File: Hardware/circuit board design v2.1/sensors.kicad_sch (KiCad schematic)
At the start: 10 parts, among them U4 BME280, U8 BMI088, U9 LIS3MDLTR

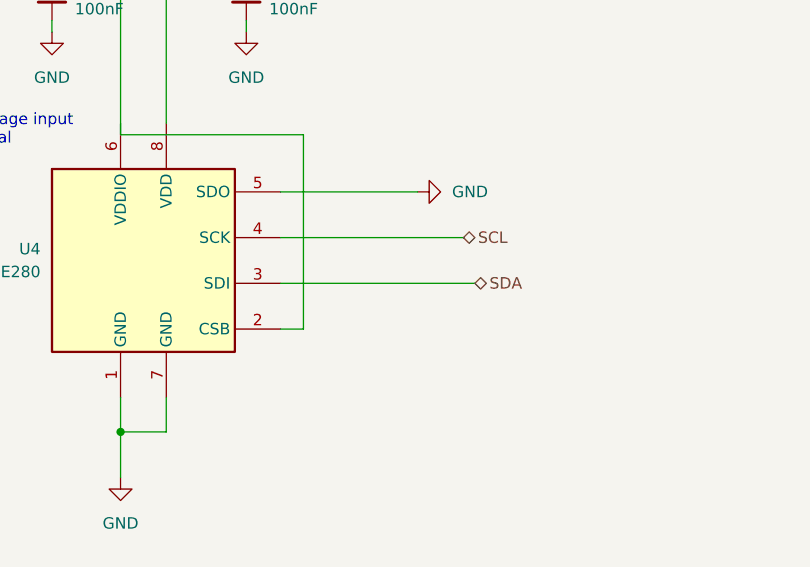
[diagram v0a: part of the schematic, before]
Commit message: Found error transistor pinout
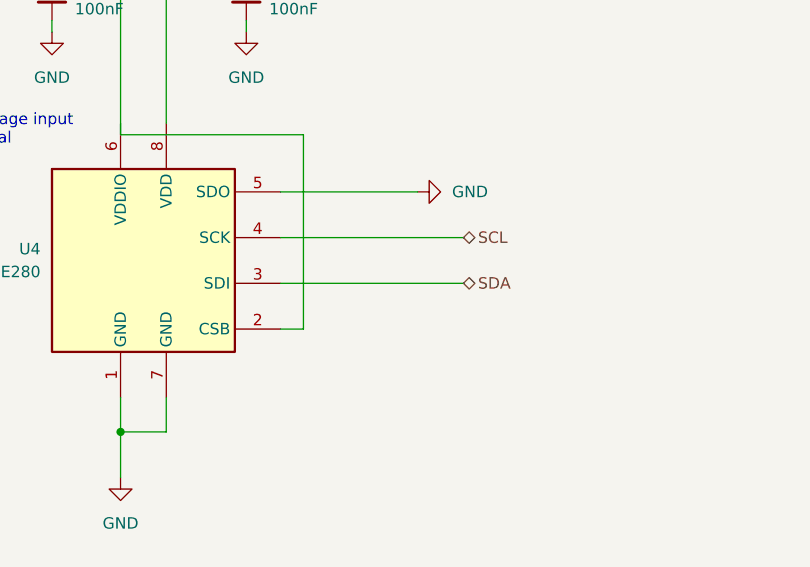
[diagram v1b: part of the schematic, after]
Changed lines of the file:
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@@
     (stroke (width 0) (type default) (color 0 0 0 0))
   )
-  (wire (pts (xy 73.66 67.31) (xy 95.25 67.31))
+  (wire (pts (xy 73.66 67.31) (xy 93.98 67.31))
     (stroke (width 0) (type default) (color 0 0 0 0))
   )
@@
     (effects (font (size 1.27 1.27)) (justify left))
   )
-  (hierarchical_label "SDA" (shape bidirectional) (at 95.25 67.31 0)
+  (hierarchical_label "SDA" (shape bidirectional) (at 93.98 67.31 0)
     (effects (font (size 1.27 1.27)) (justify left))
   )

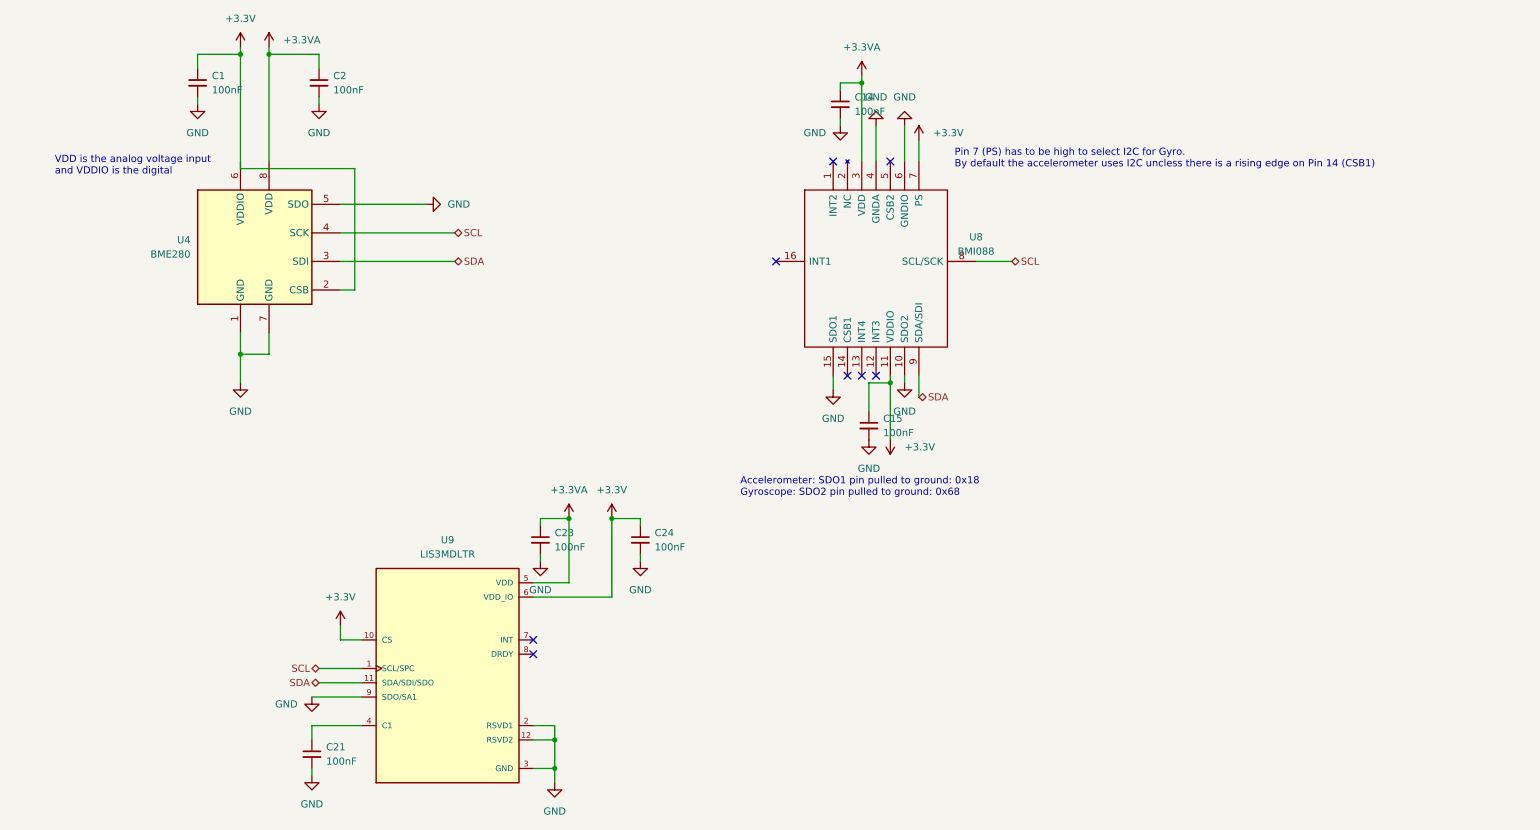
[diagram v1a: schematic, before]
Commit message: Added interupt pins to from BMI088 and LIS
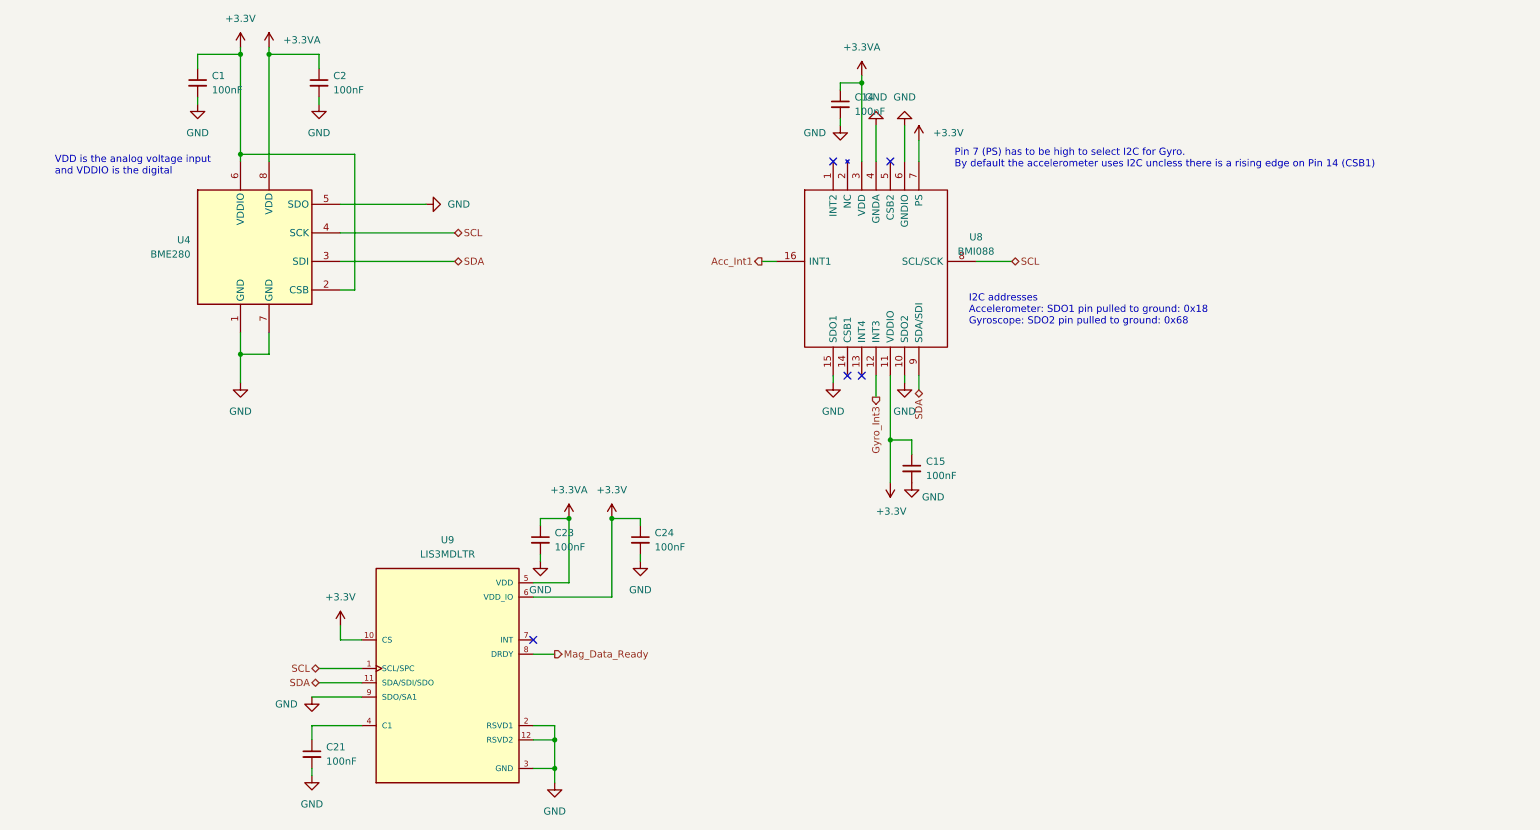
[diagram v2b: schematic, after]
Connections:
- net +3.3V: now also U4.6 (VDDIO)
- net Gyro_Int3: now reaches U8.12 (INT3)
- net Acc_Int1: now reaches U8.16 (INT1)
- net Mag_Data_Ready: now reaches U9.8 (DRDY)
- no-connect marks 8 -> 5
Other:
- note added: "I2C addresses Accelerometer: SDO1 pin pulled to ground: 0x18 Gyroscope: SDO2 pin pulled to ground: 0x68"
- note removed: "Accelerometer: SDO1 pin pulled to ground: 0x18 Gyroscope: SDO2 pin pulled to ground: 0x68"
- moved on the sheet: C15
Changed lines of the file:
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@@
   (junction (at 114.3 113.03) (diameter 0) (color 0 0 0 0)
   )
+  (junction (at 55.88 48.26) (diameter 0) (color 0 0 0 0)
+  )
   (junction (at 111.76 152.4) (diameter 0) (color 0 0 0 0)
   )
   (junction (at 55.88 83.82) (diameter 0) (color 0 0 0 0)
   )
+  (junction (at 171.45 99.06) (diameter 0) (color 0 0 0 0)
+  )
   (junction (at 121.92 113.03) (diameter 0) (color 0 0 0 0)
   )
-  (junction (at 171.45 88.9) (diameter 0) (color 0 0 0 0)
-  )
   (junction (at 111.76 157.48) (diameter 0) (color 0 0 0 0)
   )
@@
   )
   (no_connect (at 107.95 134.62))
-  (no_connect (at 107.95 137.16))
   (no_connect (at 166.37 87.63))
-  (no_connect (at 151.13 67.31))
-  (no_connect (at 168.91 87.63))
   (no_connect (at 163.83 87.63))
   (no_connect (at 171.45 49.53))
   (no_connect (at 161.29 49.53))
-  (wire (pts (xy 171.45 88.9) (xy 171.45 99.06))
+  (wire (pts (xy 148.59 67.31) (xy 151.13 67.31))
     (stroke (width 0) (type default) (color 0 0 0 0))
   )
@@
     (stroke (width 0) (type default) (color 0 0 0 0))
   )
-  (wire (pts (xy 171.45 87.63) (xy 171.45 88.9))
+  (wire (pts (xy 171.45 87.63) (xy 171.45 99.06))
     (stroke (width 0) (type default) (color 0 0 0 0))
   )
@@
     (stroke (width 0) (type default) (color 0 0 0 0))
   )
+  (wire (pts (xy 55.88 48.26) (xy 55.88 49.53))
+    (stroke (width 0) (type default) (color 0 0 0 0))
+  )
   (wire (pts (xy 127 120.65) (xy 127 119.38))
     (stroke (width 0) (type default) (color 0 0 0 0))
@@
     (stroke (width 0) (type default) (color 0 0 0 0))
   )
+  (wire (pts (xy 168.91 87.63) (xy 168.91 91.44))
+    (stroke (width 0) (type default) (color 0 0 0 0))
+  )
   (wire (pts (xy 60.96 80.01) (xy 60.96 83.82))
     (stroke (width 0) (type default) (color 0 0 0 0))
@@
     (stroke (width 0) (type default) (color 0 0 0 0))
   )
-  (wire (pts (xy 55.88 30.48) (xy 55.88 50.8))
+  (wire (pts (xy 171.45 99.06) (xy 171.45 106.68))
+    (stroke (width 0) (type default) (color 0 0 0 0))
+  )
+  (wire (pts (xy 55.88 30.48) (xy 55.88 48.26))
     (stroke (width 0) (type default) (color 0 0 0 0))
   )
@@
     (stroke (width 0) (type default) (color 0 0 0 0))
   )
+  (wire (pts (xy 107.95 137.16) (xy 111.76 137.16))
+    (stroke (width 0) (type default) (color 0 0 0 0))
+  )
   (wire (pts (xy 73.66 67.31) (xy 93.98 67.31))
     (stroke (width 0) (type default) (color 0 0 0 0))
@@
     (stroke (width 0) (type default) (color 0 0 0 0))
   )
-  (wire (pts (xy 55.88 50.8) (xy 76.2 50.8))
+  (wire (pts (xy 55.88 48.26) (xy 76.2 48.26))
     (stroke (width 0) (type default) (color 0 0 0 0))
   )
@@
     (stroke (width 0) (type default) (color 0 0 0 0))
   )
-  (wire (pts (xy 176.53 87.63) (xy 176.53 91.44))
+  (wire (pts (xy 176.53 87.63) (xy 176.53 90.17))
     (stroke (width 0) (type default) (color 0 0 0 0))
   )
@@
     (stroke (width 0) (type default) (color 0 0 0 0))
   )
-  (wire (pts (xy 161.29 87.63) (xy 161.29 90.17))
+  (wire (pts (xy 161.29 87.63) (xy 161.29 88.9))
     (stroke (width 0) (type default) (color 0 0 0 0))
   )
@@
     (stroke (width 0) (type default) (color 0 0 0 0))
   )
-  (wire (pts (xy 167.64 88.9) (xy 171.45 88.9))
+  (wire (pts (xy 171.45 99.06) (xy 175.26 99.06))
     (stroke (width 0) (type default) (color 0 0 0 0))
   )
@@
     (stroke (width 0) (type default) (color 0 0 0 0))
   )
+  (wire (pts (xy 175.26 99.06) (xy 175.26 101.6))
+    (stroke (width 0) (type default) (color 0 0 0 0))
+  )
   (wire (pts (xy 55.88 83.82) (xy 60.96 83.82))
     (stroke (width 0) (type default) (color 0 0 0 0))
   )
-  (wire (pts (xy 76.2 72.39) (xy 76.2 50.8))
+  (wire (pts (xy 76.2 72.39) (xy 76.2 48.26))
     (stroke (width 0) (type default) (color 0 0 0 0))
   )
@@
   )
   (wire (pts (xy 186.69 67.31) (xy 193.04 67.31))
-    (stroke (width 0) (type default) (color 0 0 0 0))
-  )
-  (wire (pts (xy 167.64 88.9) (xy 167.64 93.98))
     (stroke (width 0) (type default) (color 0 0 0 0))
   )
@@
     (effects (font (size 1.27 1.27)) (justify left bottom))
   )
-  (text "Accelerometer: SDO1 pin pulled to ground: 0x18\nGyroscope: SDO2 pin pulled to ground: 0x68"
-    (at 144.78 109.22 0)
+  (text "I2C addresses\nAccelerometer: SDO1 pin pulled to ground: 0x18\nGyroscope: SDO2 pin pulled to ground: 0x68"
+    (at 185.42 78.74 0)
     (effects (font (size 1.27 1.27)) (justify left bottom))
   )
@@
     (effects (font (size 1.27 1.27)) (justify left))
   )
-  (hierarchical_label "SDA" (shape bidirectional) (at 176.53 91.44 0)
-    (effects (font (size 1.27 1.27)) (justify left))
+  (hierarchical_label "SDA" (shape bidirectional) (at 176.53 90.17 270)
+    (effects (font (size 1.27 1.27)) (justify right))
   )
   (hierarchical_label "SCL" (shape bidirectional) (at 69.85 139.7 180)
     (effects (font (size 1.27 1.27)) (justify right))
   )
+  (hierarchical_label "Acc_Int1" (shape output) (at 148.59 67.31 180)
+    (effects (font (size 1.27 1.27)) (justify right))
+  )
   (hierarchical_label "SDA" (shape bidirectional) (at 69.85 142.24 180)
     (effects (font (size 1.27 1.27)) (justify right))
   )
+  (hierarchical_label "Gyro_Int3" (shape output) (at 168.91 91.44 270)
+    (effects (font (size 1.27 1.27)) (justify right))
+  )
   (hierarchical_label "SCL" (shape bidirectional) (at 193.04 67.31 0)
     (effects (font (size 1.27 1.27)) (justify left))
   )
+  (hierarchical_label "Mag_Data_Ready" (shape output) (at 111.76 137.16 0)
+    (effects (font (size 1.27 1.27)) (justify left))
+  )
   (hierarchical_label "SDA" (shape bidirectional) (at 93.98 67.31 0)
     (effects (font (size 1.27 1.27)) (justify left))
@@
     (pin "2")
   )
-  (symbol (lib_id "power:+3.3V") (at 171.45 99.06 180) (unit 1)
-    (in_bom yes) (on_board yes) (fields_autoplaced)
-    (property "Reference" "#PWR0137" (id 0) (at 171.45 95.25 0)
-      (effects (font (size 1.27 1.27)) hide)
-    )
-    (property "Value" "+3.3V" (id 1) (at 173.99 100.3299 0)
+  (symbol (lib_id "power:+3.3V") (at 171.45 106.68 180) (unit 1)
+    (in_bom yes) (on_board yes)
+    (property "Reference" "#PWR0137" (id 0) (at 171.45 102.87 0)
+      (effects (font (size 1.27 1.27)) hide)
+    )
+    (property "Value" "+3.3V" (id 1) (at 168.91 111.76 0)
       (effects (font (size 1.27 1.27)) (justify right))
     )
-    (property "Footprint" "" (id 2) (at 171.45 99.06 0)
-      (effects (font (size 1.27 1.27)) hide)
-    )
-    (property "Datasheet" "" (id 3) (at 171.45 99.06 0)
+    (property "Footprint" "" (id 2) (at 171.45 106.68 0)
+      (effects (font (size 1.27 1.27)) hide)
+    )
+    (property "Datasheet" "" (id 3) (at 171.45 106.68 0)
       (effects (font (size 1.27 1.27)) hide)
     )
@@
     (pin "2")
   )
-  (symbol (lib_id "power:GND") (at 167.64 99.06 0) (unit 1)
-    (in_bom yes) (on_board yes) (fields_autoplaced)
-    (property "Reference" "#PWR0136" (id 0) (at 167.64 105.41 0)
-      (effects (font (size 1.27 1.27)) hide)
-    )
-    (property "Value" "GND" (id 1) (at 167.64 104.14 0))
-    (property "Footprint" "" (id 2) (at 167.64 99.06 0)
-      (effects (font (size 1.27 1.27)) hide)
-    )
-    (property "Datasheet" "" (id 3) (at 167.64 99.06 0)
+  (symbol (lib_id "power:GND") (at 175.26 106.68 0) (unit 1)
+    (in_bom yes) (on_board yes)
+    (property "Reference" "#PWR0136" (id 0) (at 175.26 113.03 0)
+      (effects (font (size 1.27 1.27)) hide)
+    )
+    (property "Value" "GND" (id 1) (at 179.07 109.22 0))
+    (property "Footprint" "" (id 2) (at 175.26 106.68 0)
+      (effects (font (size 1.27 1.27)) hide)
+    )
+    (property "Datasheet" "" (id 3) (at 175.26 106.68 0)
       (effects (font (size 1.27 1.27)) hide)
     )
@@
     (pin "9")
   )
-  (symbol (lib_id "power:GND") (at 161.29 90.17 0) (unit 1)
-    (in_bom yes) (on_board yes) (fields_autoplaced)
-    (property "Reference" "#PWR0135" (id 0) (at 161.29 96.52 0)
-      (effects (font (size 1.27 1.27)) hide)
-    )
-    (property "Value" "GND" (id 1) (at 161.29 95.25 0))
-    (property "Footprint" "" (id 2) (at 161.29 90.17 0)
-      (effects (font (size 1.27 1.27)) hide)
-    )
-    (property "Datasheet" "" (id 3) (at 161.29 90.17 0)
+  (symbol (lib_id "power:GND") (at 161.29 88.9 0) (unit 1)
+    (in_bom yes) (on_board yes) (fields_autoplaced)
+    (property "Reference" "#PWR0135" (id 0) (at 161.29 95.25 0)
+      (effects (font (size 1.27 1.27)) hide)
+    )
+    (property "Value" "GND" (id 1) (at 161.29 93.98 0))
+    (property "Footprint" "" (id 2) (at 161.29 88.9 0)
+      (effects (font (size 1.27 1.27)) hide)
+    )
+    (property "Datasheet" "" (id 3) (at 161.29 88.9 0)
       (effects (font (size 1.27 1.27)) hide)
     )
@@
     (pin "8")
   )
-  (symbol (lib_id "Components:C_0603") (at 167.64 96.52 0) (unit 1)
-    (in_bom yes) (on_board yes) (fields_autoplaced)
-    (property "Reference" "C15" (id 0) (at 170.18 95.2562 0)
-      (effects (font (size 1.27 1.27)) (justify left))
-    )
-    (property "Value" "100nF" (id 1) (at 170.18 97.7962 0)
-      (effects (font (size 1.27 1.27)) (justify left))
-    )
-    (property "Footprint" "Components:C_0603_1608Metric" (id 2) (at 167.64 96.52 0)
-      (effects (font (size 1.27 1.27)) hide)
-    )
-    (property "Datasheet" "~" (id 3) (at 167.64 96.52 0)
-      (effects (font (size 1.27 1.27)) hide)
-    )
+  (symbol (lib_id "Components:C_0603") (at 175.26 104.14 0) (unit 1)
+    (in_bom yes) (on_board yes) (fields_autoplaced)
+    (property "Reference" "C15" (id 0) (at 177.8 102.8762 0)
+      (effects (font (size 1.27 1.27)) (justify left))
+    )
+    (property "Value" "100nF" (id 1) (at 177.8 105.4162 0)
+      (effects (font (size 1.27 1.27)) (justify left))
+    )
+    (property "Footprint" "Components:C_0603_1608Metric" (id 2) (at 175.26 104.14 0)
+      (effects (font (size 1.27 1.27)) hide)
+    )
+    (property "Datasheet" "~" (id 3) (at 175.26 104.14 0)
+      (effects (font (size 1.27 1.27)) hide)
+    )

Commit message: PCB V2.1 sent for manufacture
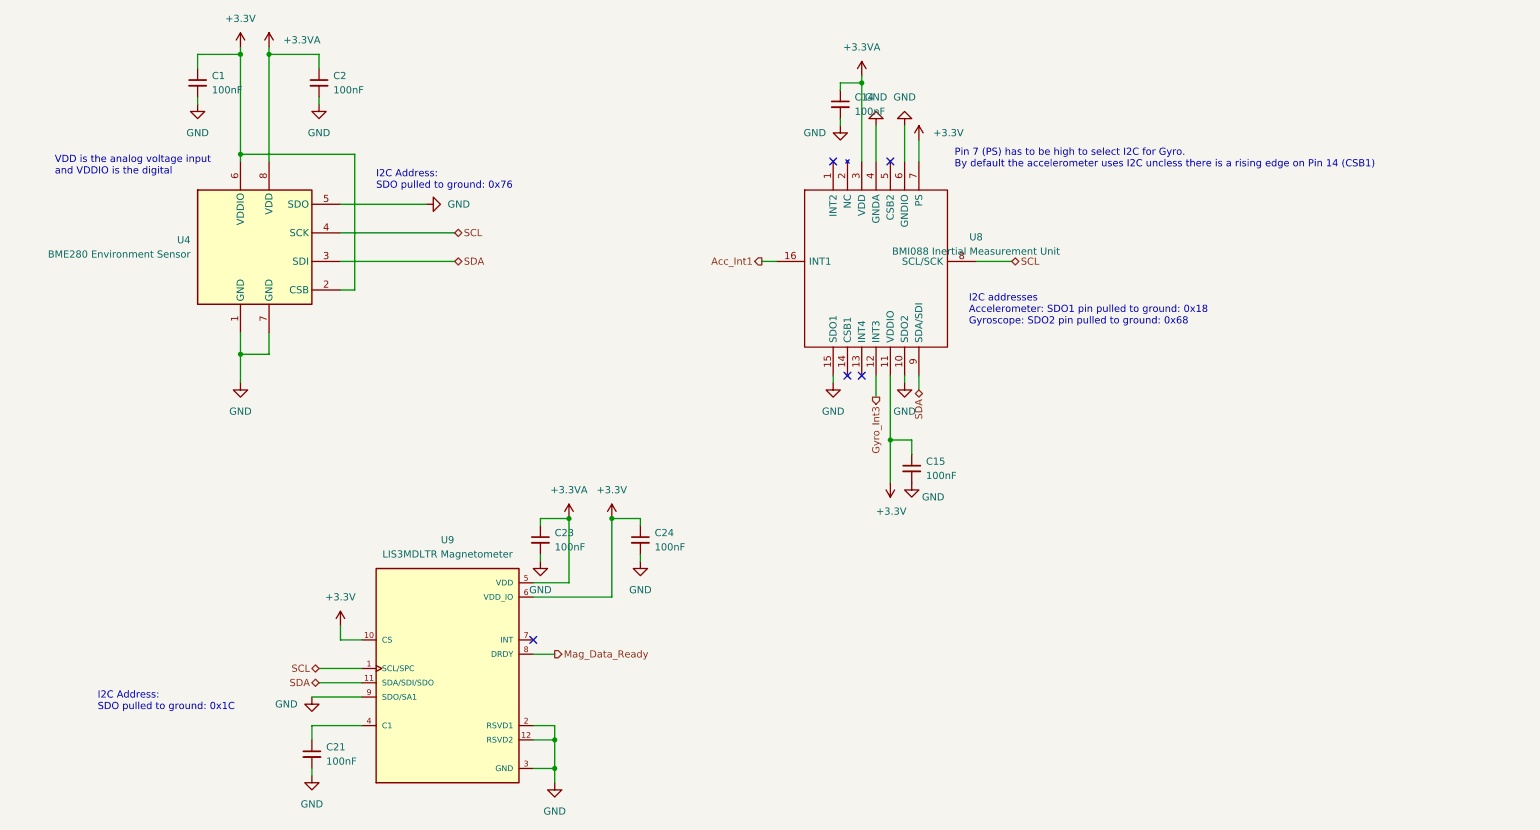
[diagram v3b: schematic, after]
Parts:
- U4: value BME280 -> BME280 Environment Sensor
- U8: value BMI088 -> BMI088 Inertial Measurement Unit
- U9: value LIS3MDLTR -> LIS3MDLTR Magnetometer
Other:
- note added: "I2C Address: SDO pulled to ground: 0x1C"
- note added: "I2C Address: SDO pulled to ground: 0x76"
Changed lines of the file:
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@@
+    (effects (font (size 1.27 1.27)) (justify left bottom))
+  )
+  (text "I2C Address:\nSDO pulled to ground: 0x1C" (at 30.48 147.32 0)
+    (effects (font (size 1.27 1.27)) (justify left bottom))
+  )
+  (text "I2C Address:\nSDO pulled to ground: 0x76" (at 80.01 54.61 0)
     (effects (font (size 1.27 1.27)) (justify left bottom))
   )
@@
     (in_bom yes) (on_board yes) (fields_autoplaced)
     (property "Reference" "U8" (id 0) (at 186.69 62.9793 0))
-    (property "Value" "BMI088" (id 1) (at 186.69 65.5193 0))
+    (property "Value" "BMI088 Inertial Measurement Unit" (id 1) (at 186.69 65.5193 0))
     (property "Footprint" "Components:BMI088" (id 2) (at 182.88 54.61 0)
       (effects (font (size 1.27 1.27)) (justify left) hide)
@@
     (in_bom yes) (on_board yes) (fields_autoplaced)
     (property "Reference" "U9" (id 0) (at 92.71 116.84 0))
-    (property "Value" "LIS3MDLTR" (id 1) (at 92.71 119.38 0))
+    (property "Value" "LIS3MDLTR Magnetometer" (id 1) (at 92.71 119.38 0))
     (property "Footprint" "Components:XDCR_LIS3MDLTR" (id 2) (at 92.71 139.7 0)
       (effects (font (size 1.27 1.27)) (justify bottom) hide)
@@
       (effects (font (size 1.27 1.27)) (justify right))
     )
-    (property "Value" "BME280" (id 1) (at 46.99 66.0399 0)
+    (property "Value" "BME280 Environment Sensor" (id 1) (at 46.99 66.0399 0)
       (effects (font (size 1.27 1.27)) (justify right))
     )
